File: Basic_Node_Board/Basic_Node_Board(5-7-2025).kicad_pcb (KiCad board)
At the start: 2 copper layers, 62.5 x 82.5 mm, 24 parts, among them J1 Conn_01x02_Pin, J2 Conn_01x02, J3 Conn_01x19_Socket, J5 Conn_01x19_Socket, U1 INA220 Current Monitor, U2 ESP32-DEVKIT-C, U3 TJA1050T/CM,118, U6 AP64060WU-7

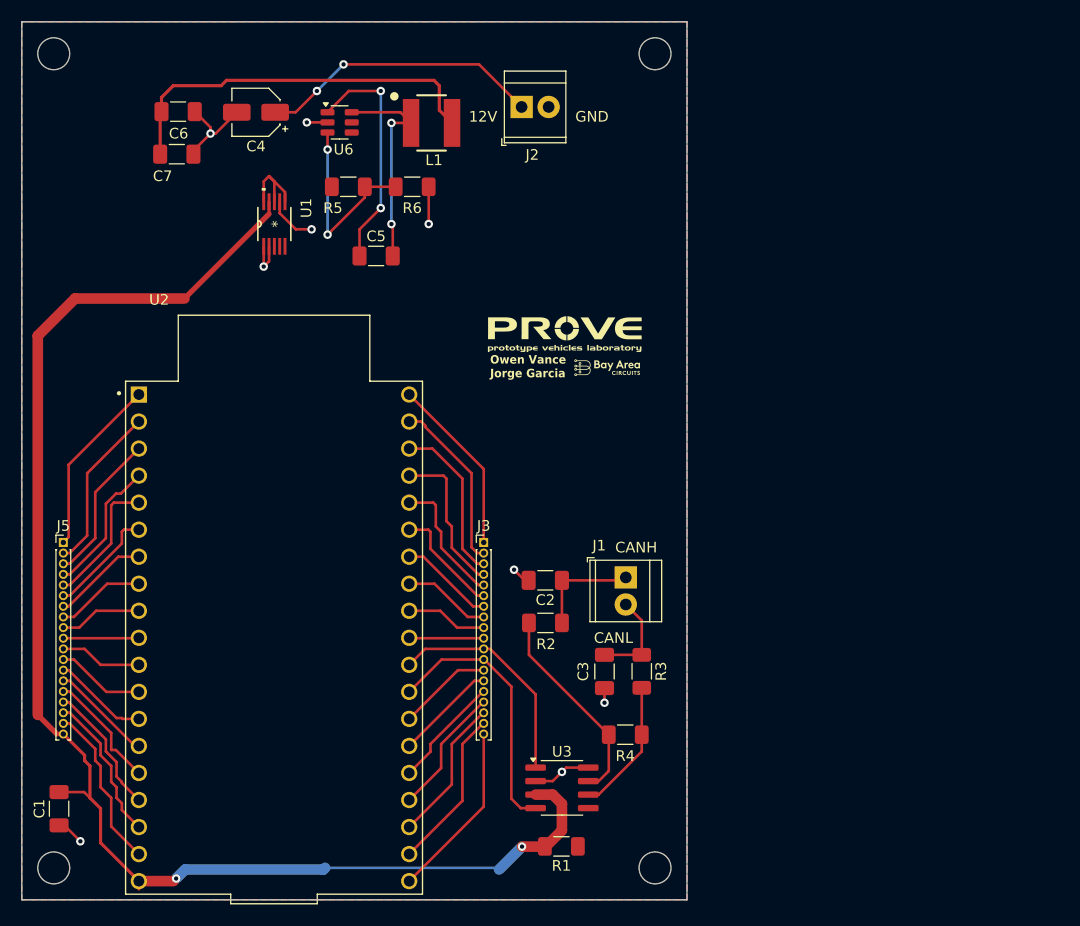
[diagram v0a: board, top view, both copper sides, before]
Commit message: initial pcb board with transciever, esp32 and can transceiver
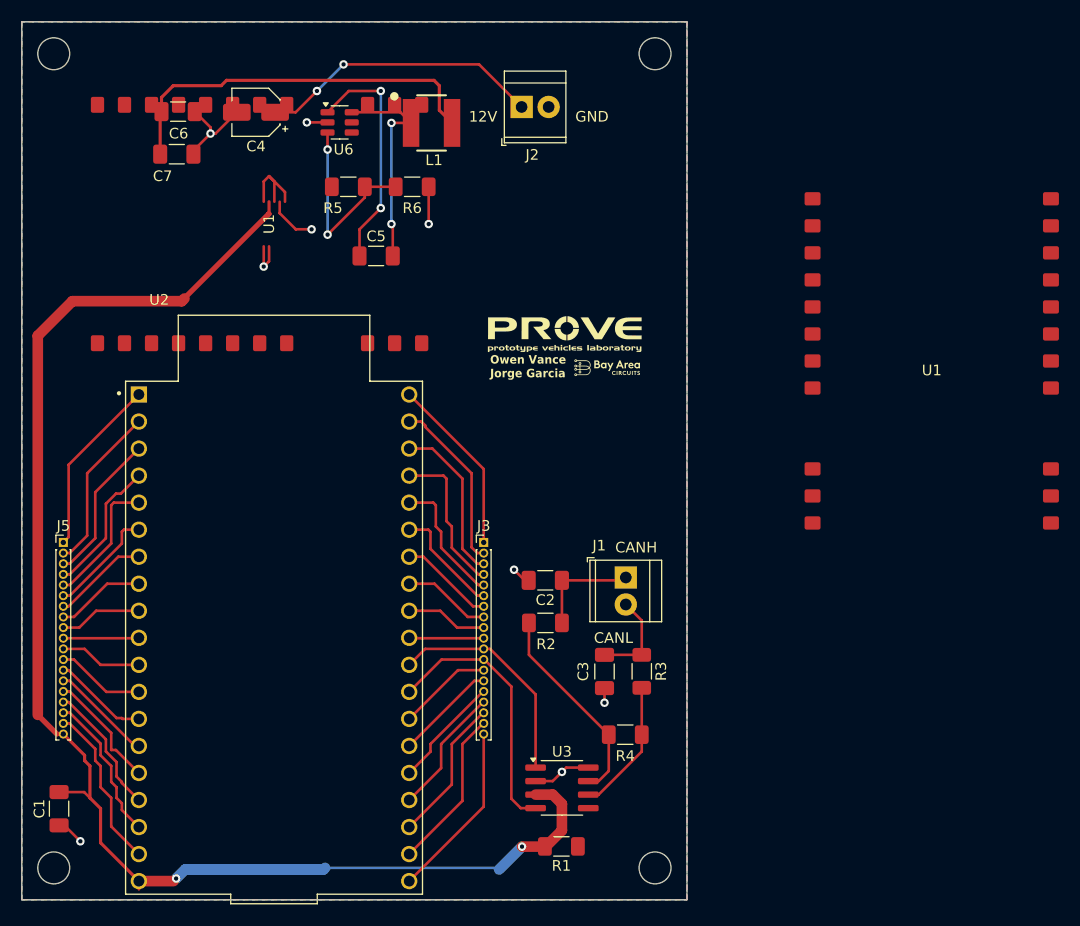
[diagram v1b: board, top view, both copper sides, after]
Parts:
- added U1: ~, Library:E22P-915M30S, F.Cu at (149.0, 82.2)
- U1: value INA220 Current Monitor -> ~; footprint PROVE:DGS10 -> Library:E22P-915M30S
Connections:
- U1 pad 1: GND -> unconnected-(U1-GND-Pad1)
- U1 pad 10: +5V -> unconnected-(U1-VCC-Pad10)
- U1 pad 2: GND -> unconnected-(U1-GND-Pad2)
- U1 pad 4: SDA -> unconnected-(U1-GND-Pad4)
- U1 pad 5: SCL -> unconnected-(U1-GND-Pad5)
- U1 pad 6: +5V -> unconnected-(U1-EN-Pad6)
- U1 pad 7: GND -> unconnected-(U1-T/R_CTRL-Pad7)
- U1 pad 8: +5V -> unconnected-(U1-DIO2-Pad8)
- U1 pad 9: +5VD -> unconnected-(U1-VCC-Pad9)
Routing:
- net unconnected-(U1-GND-Pad1): vias 0 -> 4
- net GND: vias 9 -> 5
- added copper zone on B.Cu, net unconnected-(U1-GND-Pad1)
- added copper zone on B.Cu, net unconnected-(U1-VCC-Pad10)
- added copper zone on F.Cu, net unconnected-(U1-VCC-Pad10)
- removed copper zone on F.Cu, net +5V
- removed copper zone on B.Cu, net GND
